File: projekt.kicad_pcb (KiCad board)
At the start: 4 copper layers, 65 x 65 mm, 118 parts, among them IC1 DW01+G, IC4 MIC5504-3.3YM5-TR, J1 10118194-0001LF, J10 Conn_01x06_Pin, J2 TP4056, J4 Conn_01x02_Socket, Q1 AO3420, Q2 AO3420, Q3 AO3420, Q4 AO3420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

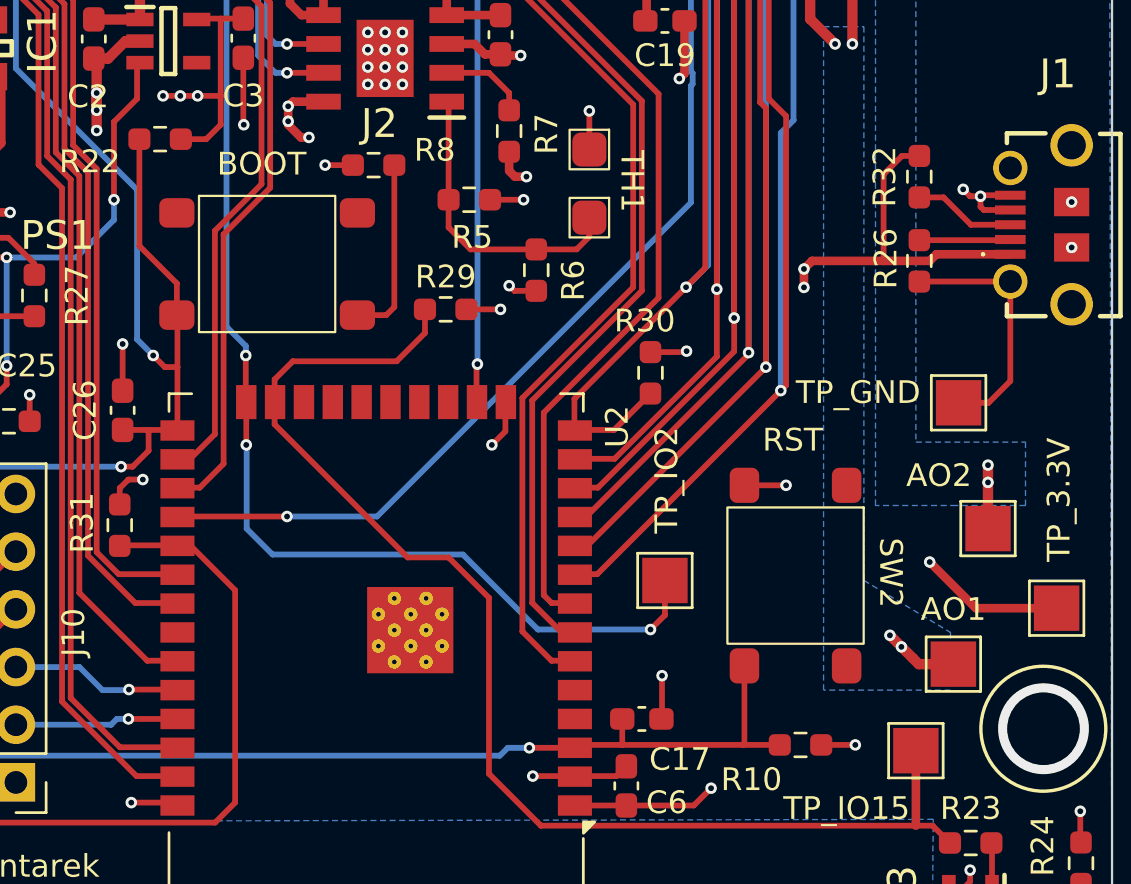
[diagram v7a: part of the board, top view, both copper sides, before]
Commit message: Podmiana przycisków
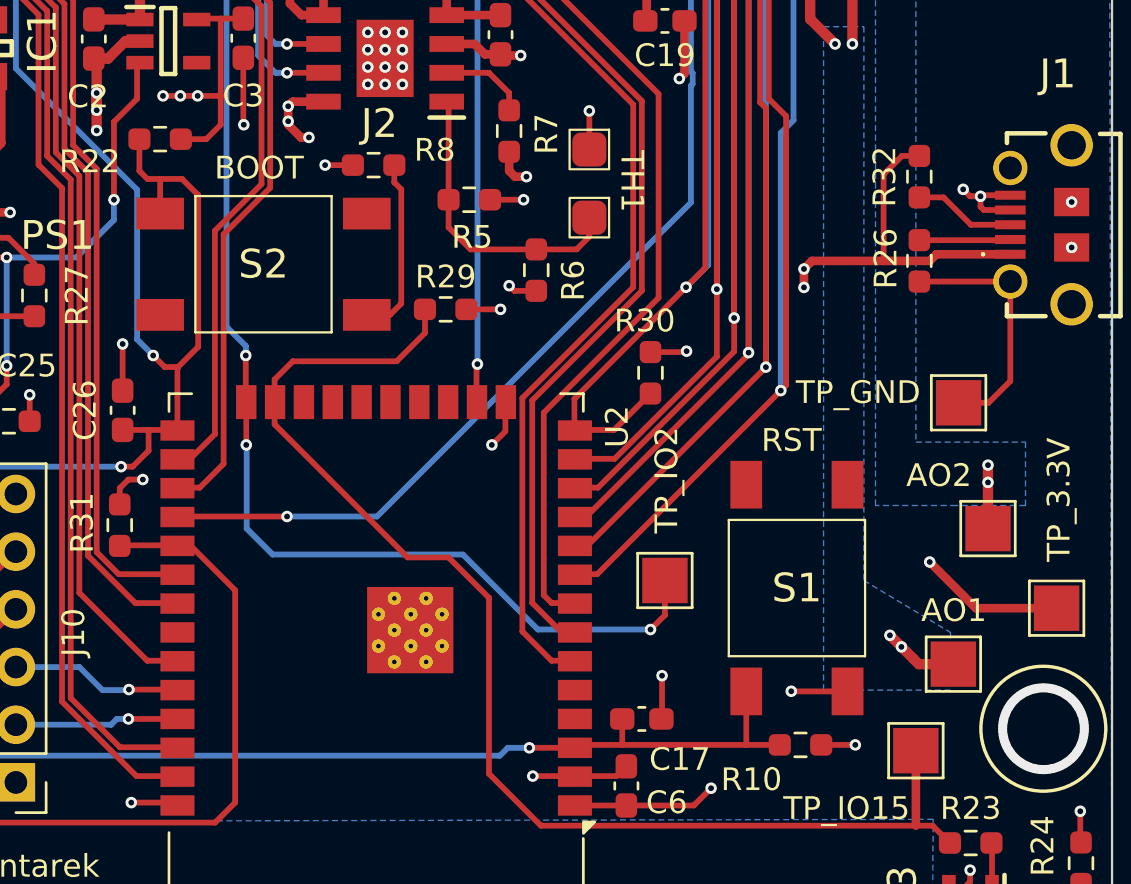
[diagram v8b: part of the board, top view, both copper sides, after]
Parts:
- removed SW2: RST, Button_Switch_SMD:TSS 62 N
- removed SW3: BOOT, Button_Switch_SMD:TSS 62 N
- added S1: 1571527-2, SamacSys_Parts:15715272, F.Cu at (167.3, 112.7)
- added S2: 1571527-2, SamacSys_Parts:15715272, F.Cu at (143.8, 98.5)
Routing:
- net /BOOT: track 81.9 -> 85.1 mm
- net /EN: track 58.0 -> 56.9 mm
- net GND: track 137.5 -> 138.1 mm
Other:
- board text added: "BOOT"
- board text added: "RST"
